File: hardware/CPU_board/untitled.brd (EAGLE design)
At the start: 128.9 x 94.9 mm, 67 parts, among them IC1 MAX232ECWE, IC2 MAX232ECWE, IC3 AM29F040J, IC4 74HCT138D, IC5 LM2596S, IC6 74245SSOP, IC7 74245SSOP, IC8 74245SSOP, J2 POWER_JACKSLT, U1 AS6C4008-55SIN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

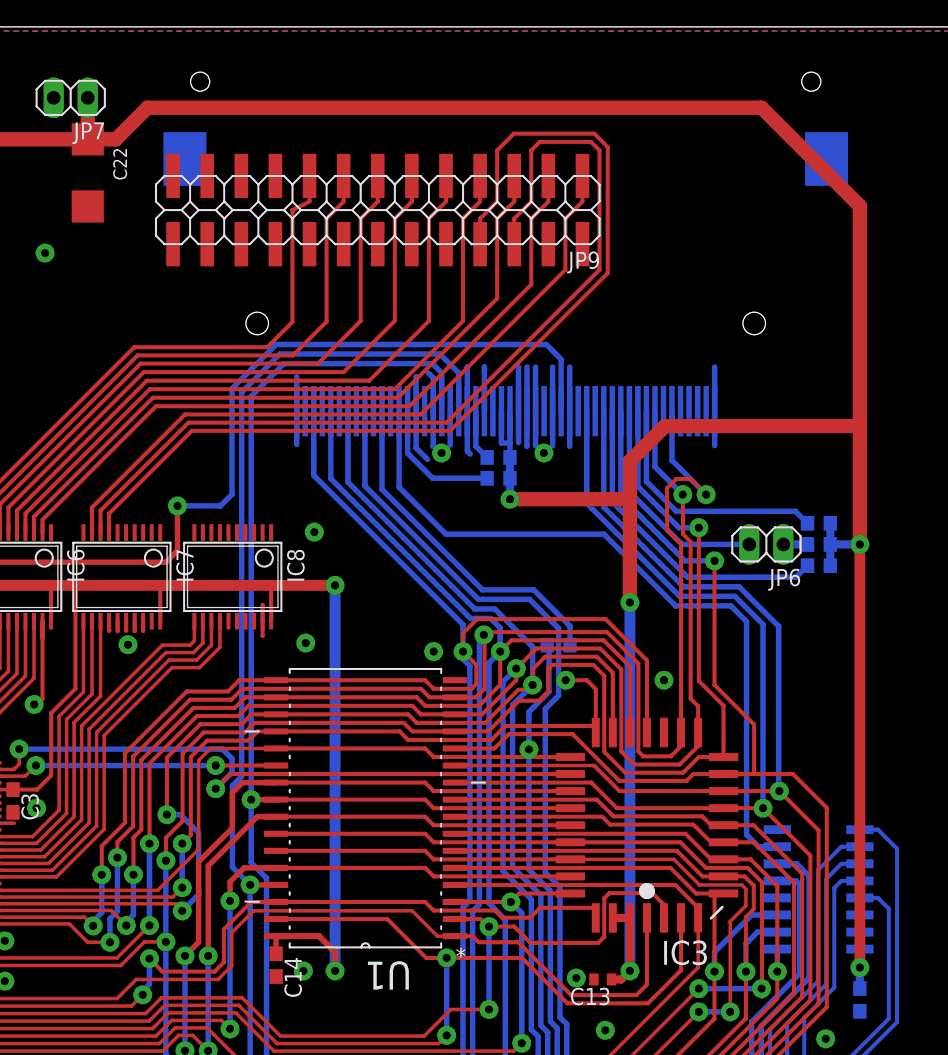
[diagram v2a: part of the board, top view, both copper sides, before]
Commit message: Printer port wired
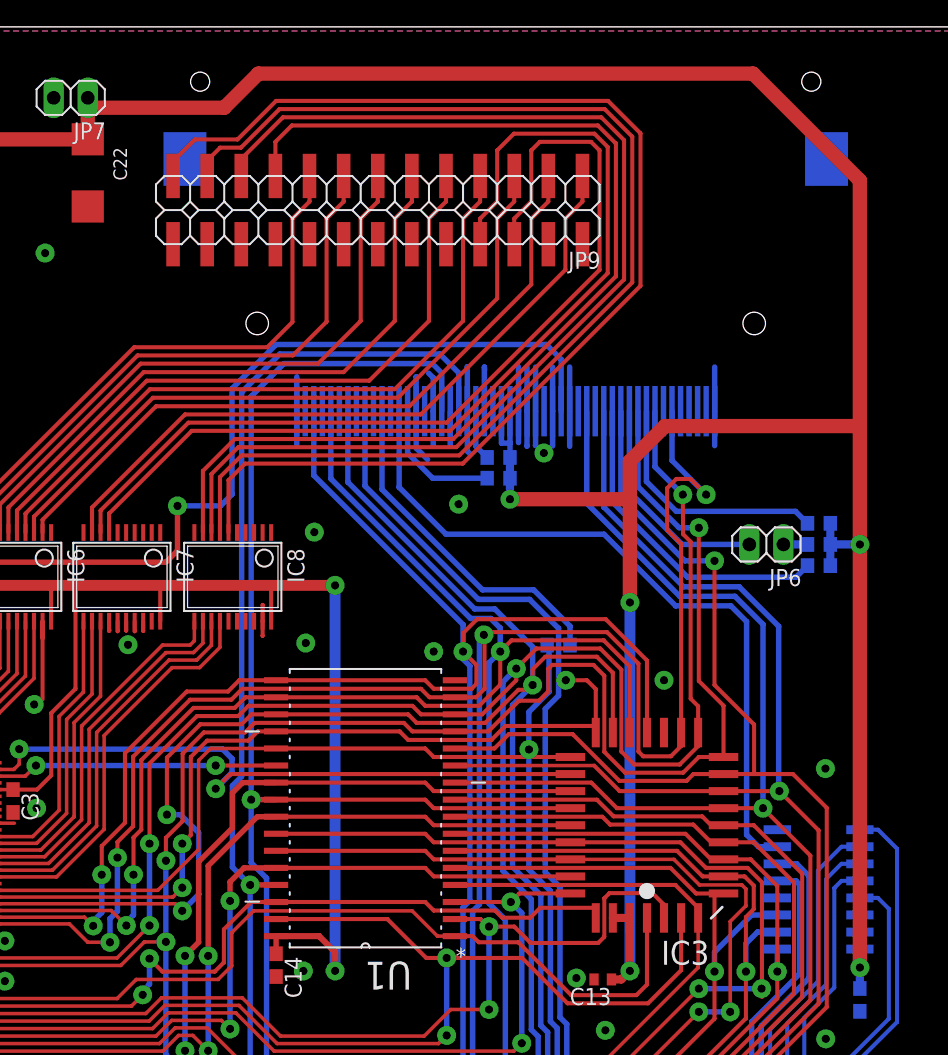
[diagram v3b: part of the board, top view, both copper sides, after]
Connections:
- net /ACK: now also IC8.9
- net BUSY: now also IC8.8
- net PE: now also IC8.7
- net SLCT: now also IC8.6
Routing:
- net SLCT: track 0.00 -> 90.7 mm
- net PE: track 0.00 -> 86.9 mm
- net BUSY: track 0.00 -> 83.2 mm
- net /ACK: track 0.00 -> 80.2 mm
- net 5V: track 502.8 -> 505.0 mm
- net GND: vias 30 -> 31
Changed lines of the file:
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@@
 <wire x1="85.4075" y1="68.1609" x2="85.0646" y2="68.5038" width="0.4064" layer="16"/>
 <via x="93.6498" y="62.5602" extent="1-16" drill="0.6" diameter="1.4224" shape="octagon"/>
-<via x="86.0298" y="62.5602" extent="1-16" drill="0.6" diameter="1.4224" shape="octagon"/>
+<via x="87.2998" y="58.7502" extent="1-16" drill="0.6" diameter="1.4224" shape="octagon"/>
 <contactref element="C21" pad="-"/>
 <contactref element="C20" pad="-"/>
@@
 <via x="75.9206" y="48.4124" extent="1-16" drill="0.6" diameter="1.4224" shape="octagon"/>
 <via x="76.5556" y="56.6674" extent="1-16" drill="0.6" diameter="1.4224" shape="octagon"/>
+<via x="114.6048" y="39.0652" extent="1-16" drill="0.6" diameter="1.4224" shape="octagon"/>
 </signal>
 <signal name="5V">
@@
 <wire x1="117.1702" y1="24.257" x2="117.1702" y2="25.6286" width="0.6096" layer="16"/>
 <wire x1="117.1702" y1="24.257" x2="117.1702" y2="22.694" width="0.6096" layer="16"/>
-<wire x1="117.1702" y1="24.257" x2="117.1702" y2="55.753" width="0.8128" layer="1"/>
+<wire x1="117.1702" y1="24.257" x2="117.1702" y2="55.753" width="1.0668" layer="1"/>
 <contactref element="R4" pad="2"/>
 <contactref element="R5" pad="2"/>
@@
 <contactref element="JP7" pad="1"/>
 <wire x1="45.2558" y1="85.9102" x2="59.69" y2="85.9102" width="1.0668" layer="1"/>
-<wire x1="59.69" y1="85.9102" x2="59.69" y2="89.0016" width="1.0668" layer="1"/>
+<wire x1="59.69" y1="85.9102" x2="59.69" y2="88.265" width="1.0668" layer="1"/>
 <contactref element="C22" pad="+"/>
+<wire x1="59.69" y1="88.265" x2="59.69" y2="89.0016" width="1.0668" layer="1"/>
 <wire x1="27.7994" y1="56.3118" x2="27.7994" y2="44.7412" width="0.8128" layer="16"/>
 <wire x1="24.13" y1="41.0718" x2="27.7994" y2="44.7412" width="0.8128" layer="16"/>
@@
 <wire x1="41.2124" y1="43.5102" x2="41.1734" y2="43.5102" width="0.6096" layer="1"/>
 <via x="91.1216" y="59.1194" extent="1-16" drill="0.6" diameter="1.4224" shape="octagon"/>
-<wire x1="59.69" y1="85.9102" x2="61.7802" y2="85.9102" width="1.0668" layer="1"/>
-<wire x1="61.7802" y1="85.9102" x2="64.135" y2="88.265" width="1.0668" layer="1"/>
-<wire x1="64.135" y1="88.265" x2="109.855" y2="88.265" width="1.0668" layer="1"/>
-<wire x1="109.855" y1="88.265" x2="117.1702" y2="80.9498" width="1.0668" layer="1"/>
+<wire x1="109.22" y1="90.805" x2="117.1702" y2="82.8548" width="1.0668" layer="1"/>
 <wire x1="117.1702" y1="55.753" x2="117.1702" y2="64.56524375" width="1.0668" layer="1"/>
-<wire x1="117.1702" y1="64.56524375" x2="117.1702" y2="80.9498" width="1.0668" layer="1"/>
+<wire x1="117.1702" y1="64.56524375" x2="117.1702" y2="82.8548" width="1.0668" layer="1"/>
 <wire x1="91.1216" y1="59.1194" x2="100.0506" y2="59.1194" width="1.0668" layer="1"/>
 <wire x1="100.0506" y1="59.1194" x2="100.0506" y2="51.435" width="1.0668" layer="1"/>
@@
 <wire x1="102.66524375" y1="64.56524375" x2="100.0506" y2="61.9506" width="1.0668" layer="1"/>
 <wire x1="100.0506" y1="59.1194" x2="100.0506" y2="61.9506" width="1.0668" layer="1"/>
+<wire x1="59.69" y1="88.265" x2="69.85" y2="88.265" width="1.0668" layer="1"/>
+<wire x1="69.85" y1="88.265" x2="72.39" y2="90.805" width="1.0668" layer="1"/>
+<wire x1="72.39" y1="90.805" x2="109.22" y2="90.805" width="1.0668" layer="1"/>
 <wire x1="59.69" y1="85.9102" x2="59.69" y2="85.9136" width="0" layer="19" extent="1-1"/>
 <wire x1="59.69" y1="8.9916" x2="50.2548" y2="23.4696" width="0" layer="19" extent="1-1"/>
@@
 <wire x1="63.1444" y1="70.4342" x2="73.0504" y2="70.4342" width="0.3048" layer="1"/>
 <wire x1="76.2" y1="83.185" x2="76.2" y2="81.28" width="0.3048" layer="1"/>
-<wire x1="76.2" y1="81.28" x2="74.93" y2="80.645" width="0.3048" layer="1"/>
-<wire x1="74.93" y1="80.645" x2="74.93" y2="72.3138" width="0.3048" layer="1"/>
+<wire x1="76.2" y1="81.28" x2="74.93" y2="80.01" width="0.3048" layer="1"/>
+<wire x1="74.93" y1="80.01" x2="74.93" y2="72.3138" width="0.3048" layer="1"/>
 <wire x1="74.93" y1="72.3138" x2="73.0504" y2="70.4342" width="0.3048" layer="1"/>
 </signal>
 <signal name="/ACK">
 <contactref element="JP9" pad="19"/>
+<contactref element="IC8" pad="9"/>
+<wire x1="68.262" y1="56.642" x2="68.262" y2="61.2262" width="0.3048" layer="1"/>
+<wire x1="68.262" y1="61.2262" x2="70.6374" y2="63.6016" width="0.3048" layer="1"/>
+<wire x1="70.6374" y1="63.6016" x2="86.8934" y2="63.6016" width="0.3048" layer="1"/>
+<wire x1="86.8934" y1="63.6016" x2="99.0092" y2="75.7174" width="0.3048" layer="1"/>
+<wire x1="99.0092" y1="75.7174" x2="99.0092" y2="85.598" width="0.3048" layer="1"/>
+<wire x1="99.0092" y1="85.598" x2="97.663" y2="86.9442" width="0.3048" layer="1"/>
+<wire x1="97.663" y1="86.9442" x2="74.8792" y2="86.9442" width="0.3048" layer="1"/>
+<wire x1="74.8792" y1="86.9442" x2="73.66" y2="85.725" width="0.3048" layer="1"/>
+<wire x1="73.66" y1="85.725" x2="73.66" y2="83.185" width="0.3048" layer="1"/>
 </signal>
 <signal name="BUSY">
 <contactref element="JP9" pad="21"/>
+<contactref element="IC8" pad="8"/>
+<wire x1="68.897" y1="56.642" x2="68.897" y2="60.9976" width="0.3048" layer="1"/>
+<wire x1="68.897" y1="60.9976" x2="70.8914" y2="62.992" width="0.3048" layer="1"/>
+<wire x1="70.8914" y1="62.992" x2="87.122" y2="62.992" width="0.3048" layer="1"/>
+<wire x1="87.122" y1="62.992" x2="99.6188" y2="75.4888" width="0.3048" layer="1"/>
+<wire x1="99.6188" y1="75.4888" x2="99.6188" y2="85.852" width="0.3048" layer="1"/>
+<wire x1="99.6188" y1="85.852" x2="97.917" y2="87.5538" width="0.3048" layer="1"/>
+<wire x1="97.917" y1="87.5538" x2="74.2188" y2="87.5538" width="0.3048" layer="1"/>
+<wire x1="74.2188" y1="87.5538" x2="71.12" y2="84.455" width="0.3048" layer="1"/>
+<wire x1="71.12" y1="83.185" x2="71.12" y2="84.455" width="0.3048" layer="1"/>
 </signal>
 <signal name="PE">
 <contactref element="JP9" pad="23"/>
+<contactref element="IC8" pad="7"/>
+<wire x1="69.532" y1="56.642" x2="69.532" y2="60.769" width="0.3048" layer="1"/>
+<wire x1="69.532" y1="60.769" x2="71.1454" y2="62.3824" width="0.3048" layer="1"/>
+<wire x1="71.1454" y1="62.3824" x2="87.3506" y2="62.3824" width="0.3048" layer="1"/>
+<wire x1="87.3506" y1="62.3824" x2="100.2284" y2="75.2602" width="0.3048" layer="1"/>
+<wire x1="100.2284" y1="75.2602" x2="100.2284" y2="86.106" width="0.3048" layer="1"/>
+<wire x1="100.2284" y1="86.106" x2="98.171" y2="88.1634" width="0.3048" layer="1"/>
+<wire x1="98.171" y1="88.1634" x2="73.9648" y2="88.1634" width="0.3048" layer="1"/>
+<wire x1="73.9648" y1="88.1634" x2="71.0946" y2="85.2932" width="0.3048" layer="1"/>
+<wire x1="71.0946" y1="85.2932" x2="69.5452" y2="85.2932" width="0.3048" layer="1"/>
+<wire x1="68.58" y1="83.185" x2="68.58" y2="84.328" width="0.3048" layer="1"/>
+<wire x1="68.58" y1="84.328" x2="69.5452" y2="85.2932" width="0.3048" layer="1"/>
 </signal>
 <signal name="SLCT">
 <contactref element="JP9" pad="25"/>
+<contactref element="IC8" pad="6"/>
+<wire x1="70.167" y1="56.642" x2="70.167" y2="60.5404" width="0.3048" layer="1"/>
+<wire x1="70.167" y1="60.5404" x2="71.3994" y2="61.7728" width="0.3048" layer="1"/>
+<wire x1="71.3994" y1="61.7728" x2="87.6046" y2="61.7728" width="0.3048" layer="1"/>
+<wire x1="87.6046" y1="61.7728" x2="100.838" y2="75.0062" width="0.3048" layer="1"/>
+<wire x1="100.838" y1="75.0062" x2="100.838" y2="86.36" width="0.3048" layer="1"/>
+<wire x1="100.838" y1="86.36" x2="98.425" y2="88.773" width="0.3048" layer="1"/>
+<wire x1="98.425" y1="88.773" x2="73.7108" y2="88.773" width="0.3048" layer="1"/>
+<wire x1="73.7108" y1="88.773" x2="70.8406" y2="85.9028" width="0.3048" layer="1"/>
+<wire x1="70.8406" y1="85.9028" x2="67.6656" y2="85.9028" width="0.3048" layer="1"/>
+<wire x1="67.6656" y1="85.9028" x2="66.04" y2="84.2772" width="0.3048" layer="1"/>
+<wire x1="66.04" y1="83.185" x2="66.04" y2="84.2772" width="0.3048" layer="1"/>
 </signal>
 <signal name="PD0_IN">

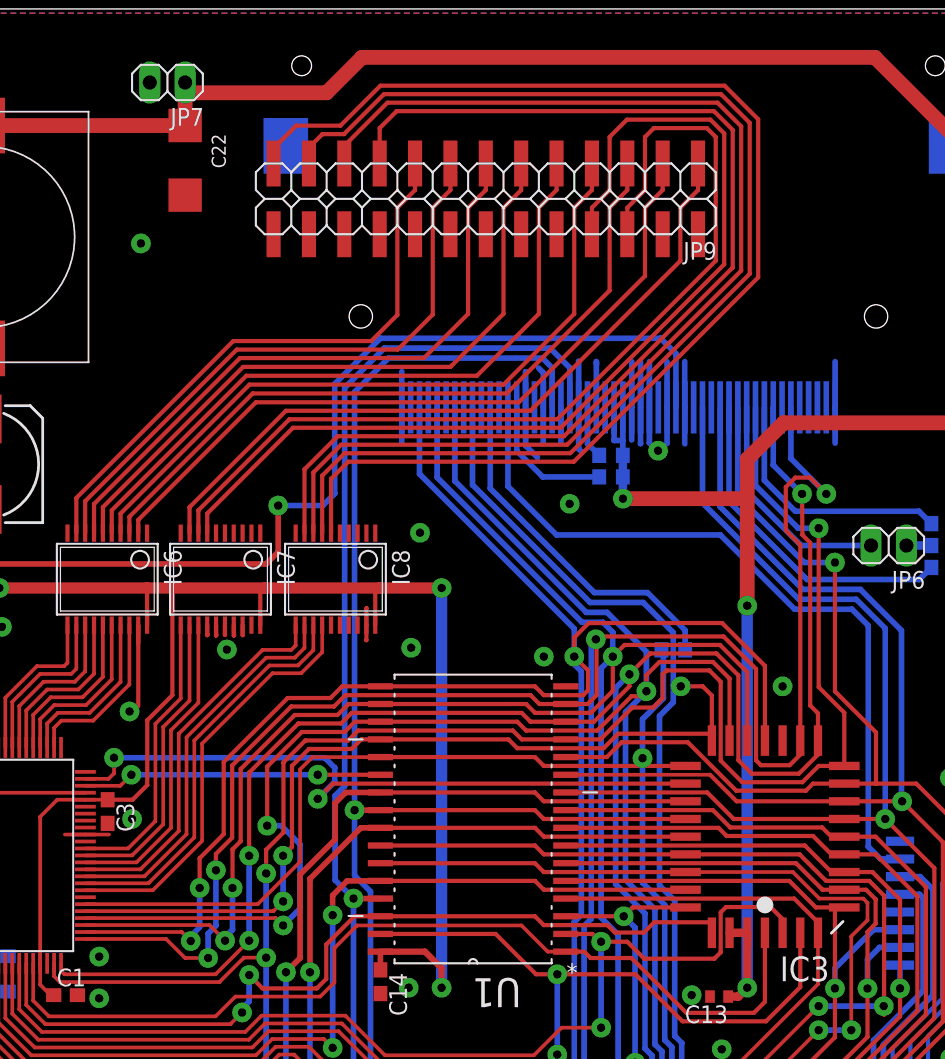
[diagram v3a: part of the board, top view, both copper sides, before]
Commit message: Printer error line routed
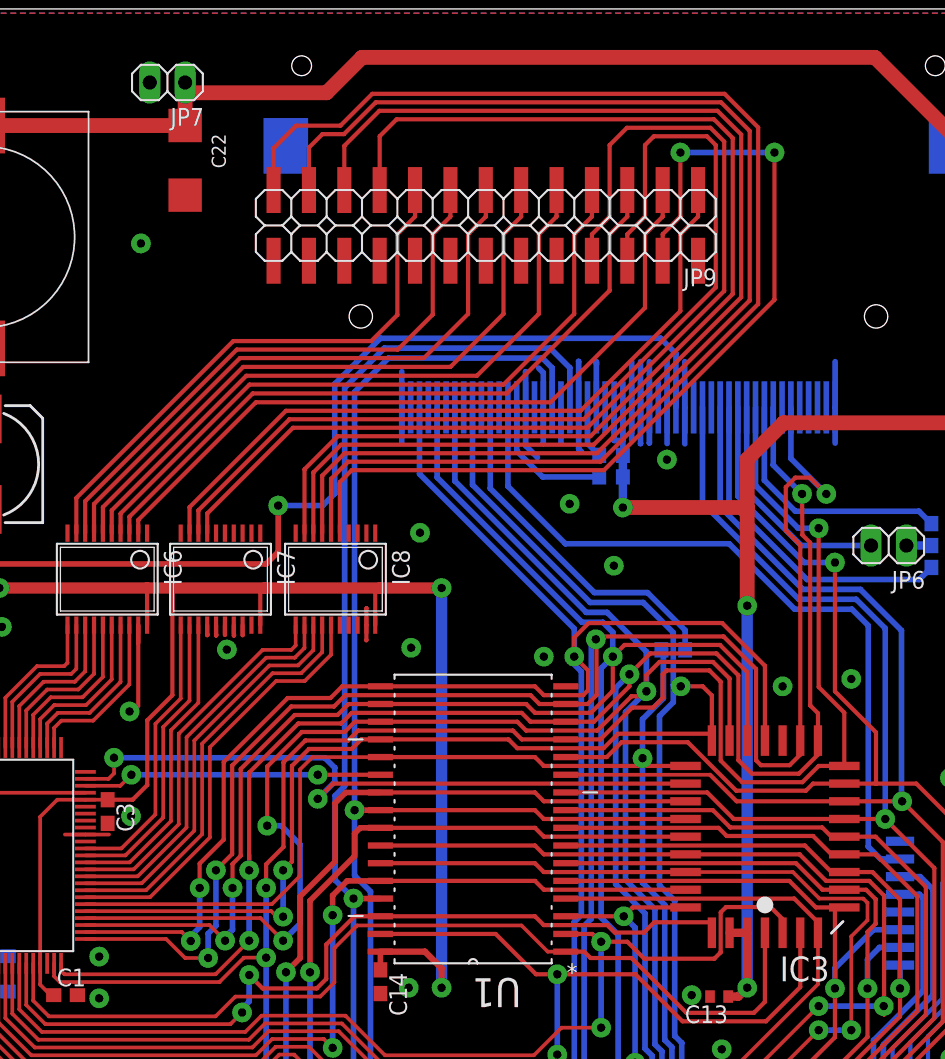
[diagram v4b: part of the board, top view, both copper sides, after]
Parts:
- moved JP9 1.91 mm to (95.2, 77.5)
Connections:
- new net /ERR_OUT: IC8.15, U$1.32
- net /ERR: now also IC8.5
- net GND: no longer IC8.5
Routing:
- net /ERR: track 0.00 -> 65.9 mm, vias 0 -> 2
- net /ERR_OUT: track 0.00 -> 30.8 mm
- net SLCT: track 90.7 -> 92.9 mm
- net PE: track 86.9 -> 89.1 mm
- net BUSY: track 83.2 -> 85.4 mm
- net PD7: track 42.4 -> 40.5 mm
- net PD6: track 44.2 -> 42.3 mm
- net PD5: track 45.9 -> 44.0 mm
- net PD4: track 47.7 -> 45.8 mm
- net PD3: track 49.5 -> 47.6 mm
- net PD2: track 51.2 -> 49.3 mm
- net PD1: track 52.0 -> 50.1 mm
- net /ACK: track 80.2 -> 82.0 mm
- net /SLIN: track 72.0 -> 73.9 mm
- net /INIT: track 68.2 -> 70.1 mm
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
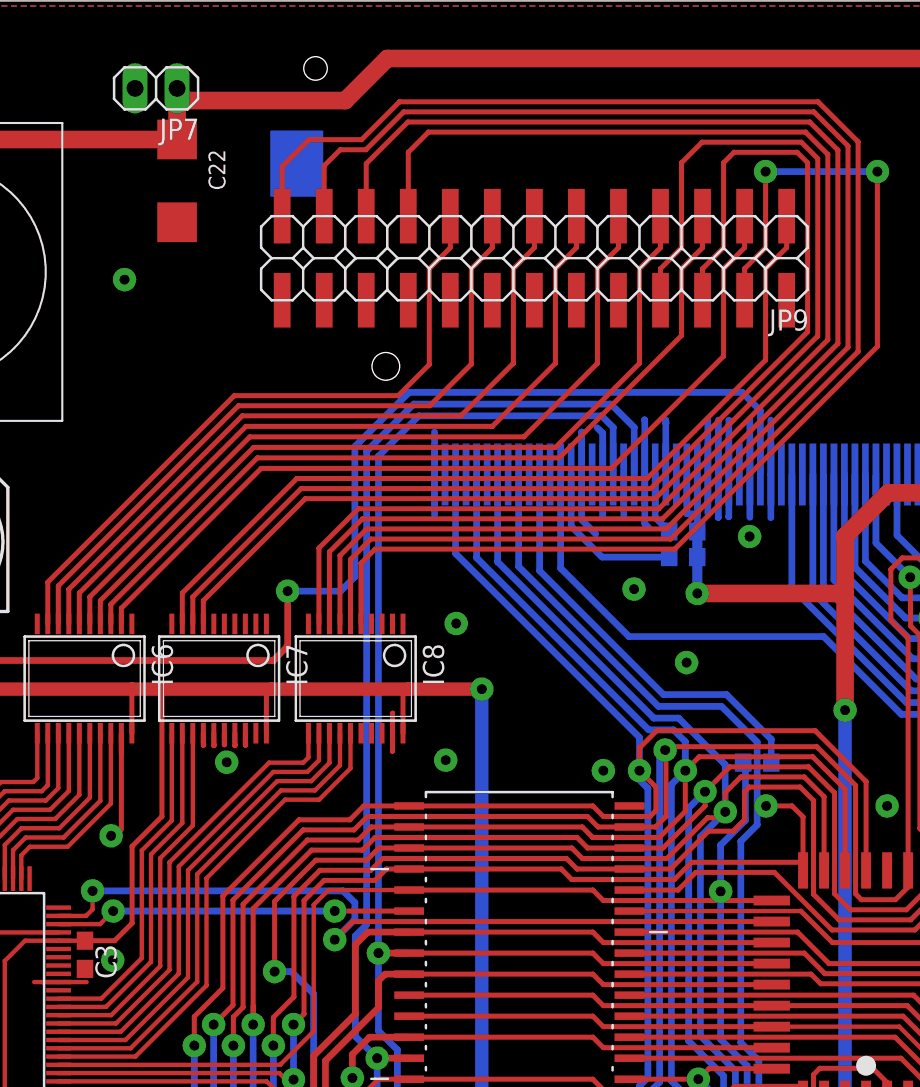
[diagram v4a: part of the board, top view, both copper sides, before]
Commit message: Capacitors added
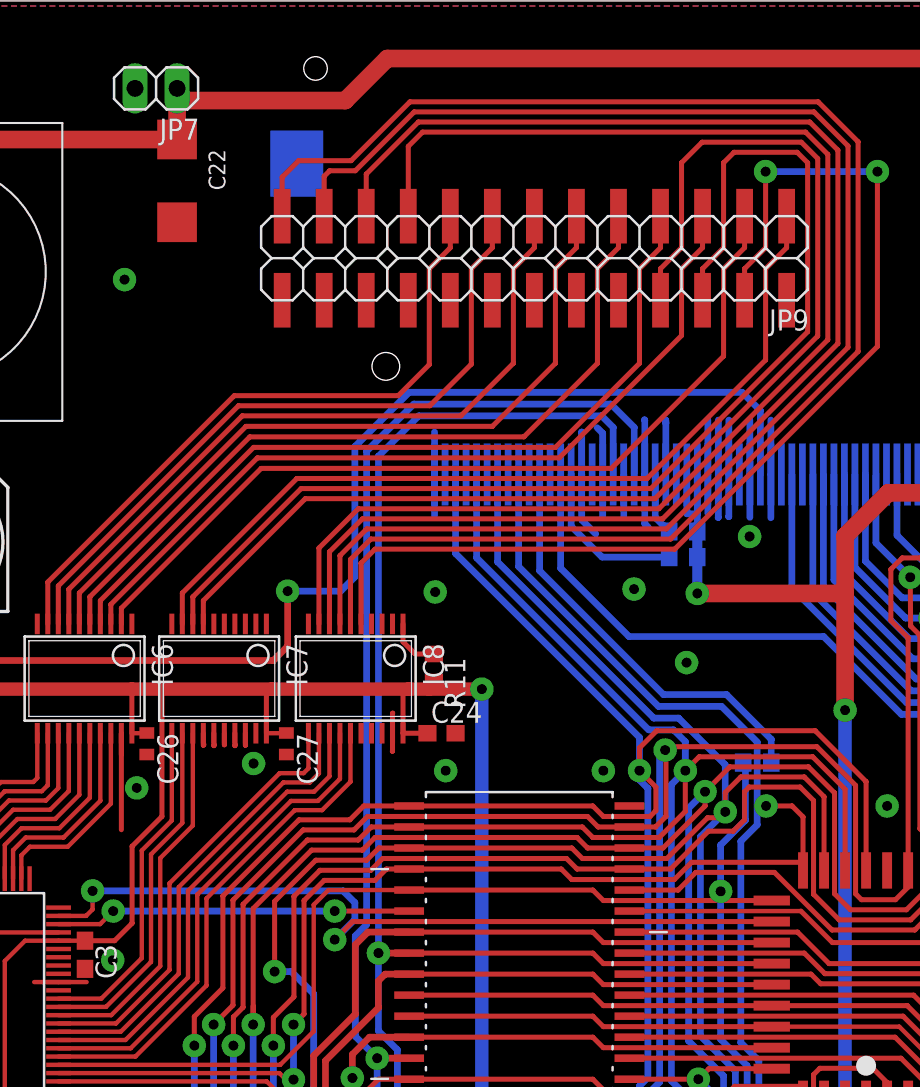
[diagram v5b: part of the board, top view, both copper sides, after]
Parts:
- added C24: (no value), rcl:C0603
- added C26, C27: (no value), rcl:C0402
- added R11: (no value), rcl:R0603
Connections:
- new net N$26: IC8.1, R11.1
- net 5V: now also C24.1, C26.1, C27.1, R11.2
- net GND: now also C24.2, C26.2, C27.2
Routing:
- net 5V: track 505.6 -> 509.8 mm
- net N$26: track 0.00 -> 3.25 mm
